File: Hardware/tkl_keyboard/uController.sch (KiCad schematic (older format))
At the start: 14 parts, among them J3 Conn_02x03_Odd_Even, SW1 SW_Push, U5 ATmega32U4-AU, X2 KC2016K

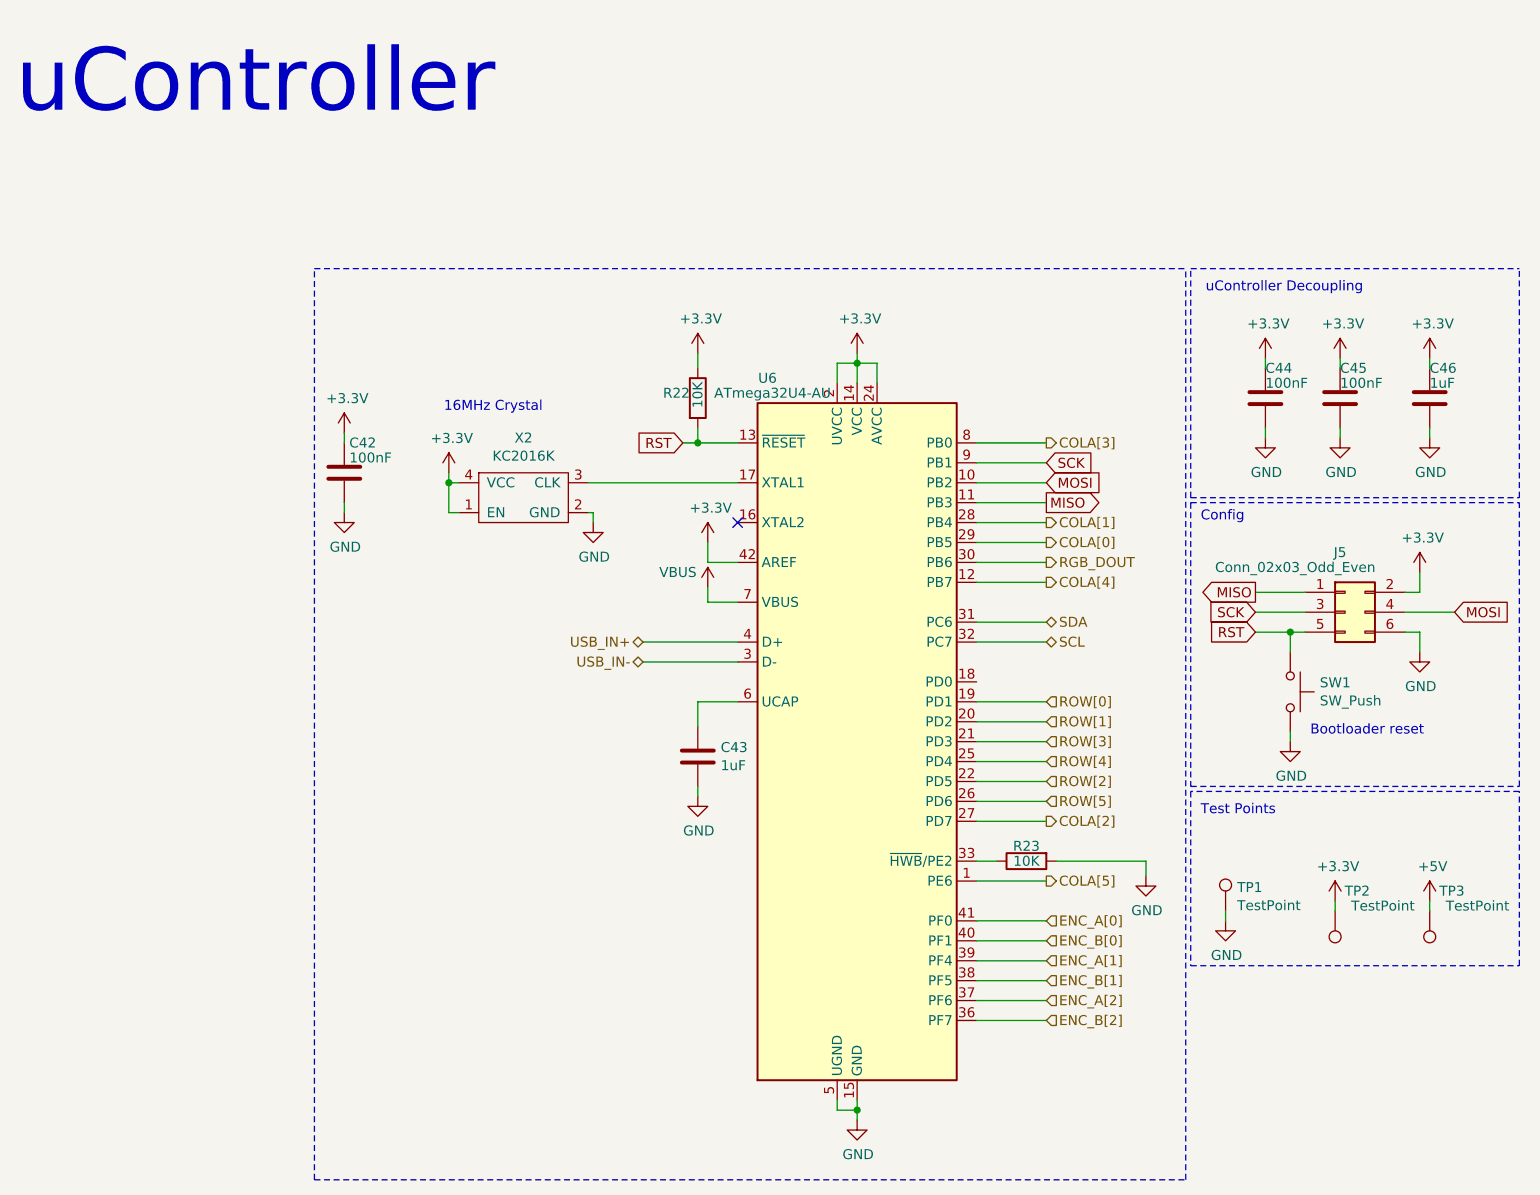
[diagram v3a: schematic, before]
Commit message: First pass of routing done
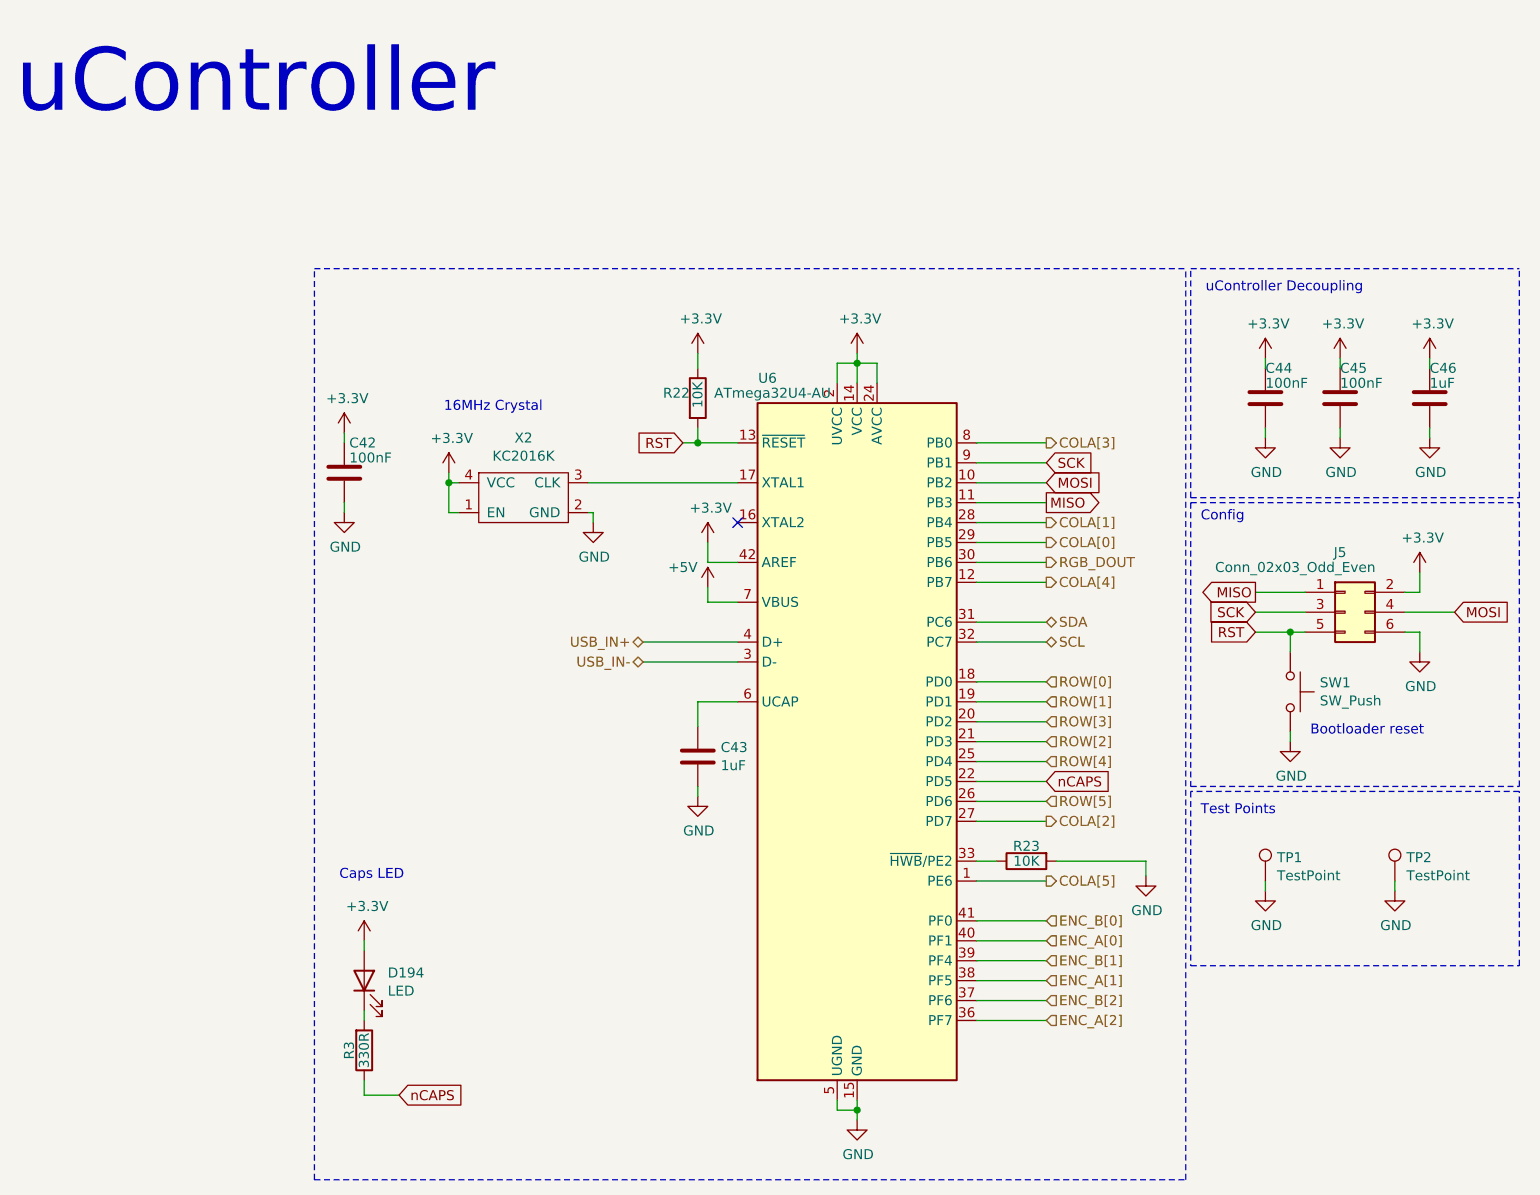
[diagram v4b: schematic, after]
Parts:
- removed TP3: TestPoint, TestPoint:TestPoint_Pad_D1.0mm, symbol Connector:TestPoint
- added D194: LED, Diode_SMD:D_0603_1608Metric, symbol Device:LED
- added R3: 330R, resistor_smd:R_0603_1608Metric, symbol Device:R
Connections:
- net VBUS is gone; now on net +5V: U5.7 (VBUS)
- net +3V3: now also D194.2 (A); no longer TP2.1
- net ENC_A[0]: now also U5.40 (PF1); no longer U5.41 (PF0)
- net ENC_A[1]: now also U5.38 (PF5); no longer U5.39 (PF4)
- net ENC_A[2]: now also U5.36 (PF7); no longer U5.37 (PF6)
- net ENC_B[0]: now also U5.41 (PF0); no longer U5.40 (PF1)
- net ENC_B[1]: now also U5.39 (PF4); no longer U5.38 (PF5)
- net ENC_B[2]: now also U5.37 (PF6); no longer U5.36 (PF7)
- net GND: now also TP2.1
- net ROW[0]: now also U5.18 (PD0); no longer U5.19 (PD1)
- net ROW[1]: now also U5.19 (PD1); no longer U5.20 (PD2)
- net ROW[2]: now also U5.21 (PD3); no longer U5.22 (PD5)
- net ROW[3]: now also U5.20 (PD2); no longer U5.21 (PD3)
- new net: D194.1 (K), R3.2
- new net nCAPS: R3.1, U5.22 (PD5)
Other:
- note added: "Caps LED"
- moved on the sheet: TP1
